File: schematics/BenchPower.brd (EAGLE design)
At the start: 79.7 x 67 mm, 28 parts, among them U1 V_REG_317SINK

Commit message: Reroute another line
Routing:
- net 5VATX: track 100.0 -> 98.9 mm
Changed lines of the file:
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@@
 <wire x1="62.865" y1="51.435" x2="62.865" y2="50.475" width="0.4064" layer="1"/>
 <wire x1="62.865" y1="50.475" x2="62.96" y2="50.38" width="0.4064" layer="1"/>
-<wire x1="60.96" y1="53.34" x2="9.525" y2="53.34" width="0.4064" layer="1"/>
 <wire x1="5.715" y1="10.61" x2="5.89" y2="10.435" width="0.4064" layer="1"/>
-<wire x1="9.525" y1="53.34" x2="6.35" y2="50.165" width="0.4064" layer="1"/>
-<wire x1="6.35" y1="50.165" x2="6.35" y2="10.895" width="0.4064" layer="1"/>
 <wire x1="6.35" y1="10.895" x2="5.89" y2="10.435" width="0.4064" layer="1"/>
+<wire x1="60.96" y1="53.34" x2="27.305" y2="53.34" width="0.4064" layer="1"/>
+<wire x1="27.305" y1="53.34" x2="23.495" y2="49.53" width="0.4064" layer="1"/>
+<wire x1="23.495" y1="49.53" x2="7.62" y2="49.53" width="0.4064" layer="1"/>
+<wire x1="7.62" y1="49.53" x2="6.35" y2="48.26" width="0.4064" layer="1"/>
+<wire x1="6.35" y1="48.26" x2="6.35" y2="10.895" width="0.4064" layer="1"/>
 </signal>
 <signal name="5V$4">

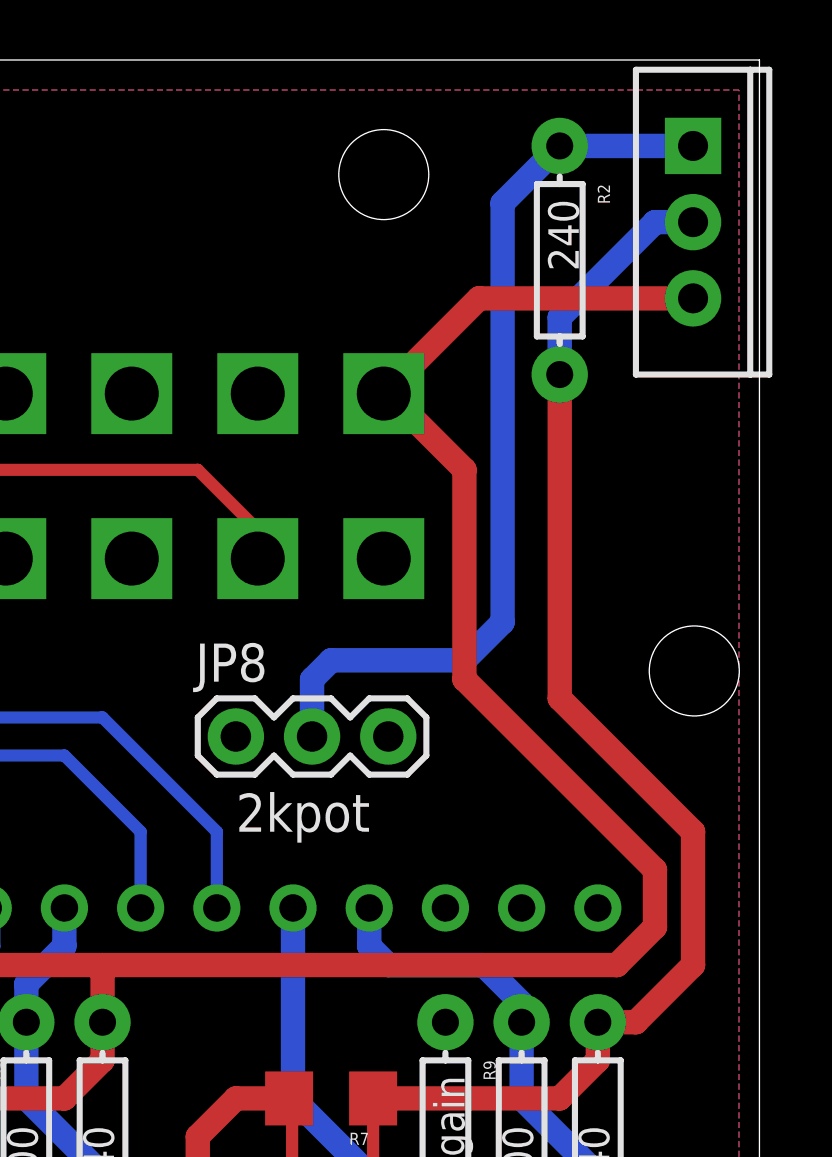
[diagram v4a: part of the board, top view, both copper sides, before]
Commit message: Make 12v or 5v selectable into regulator
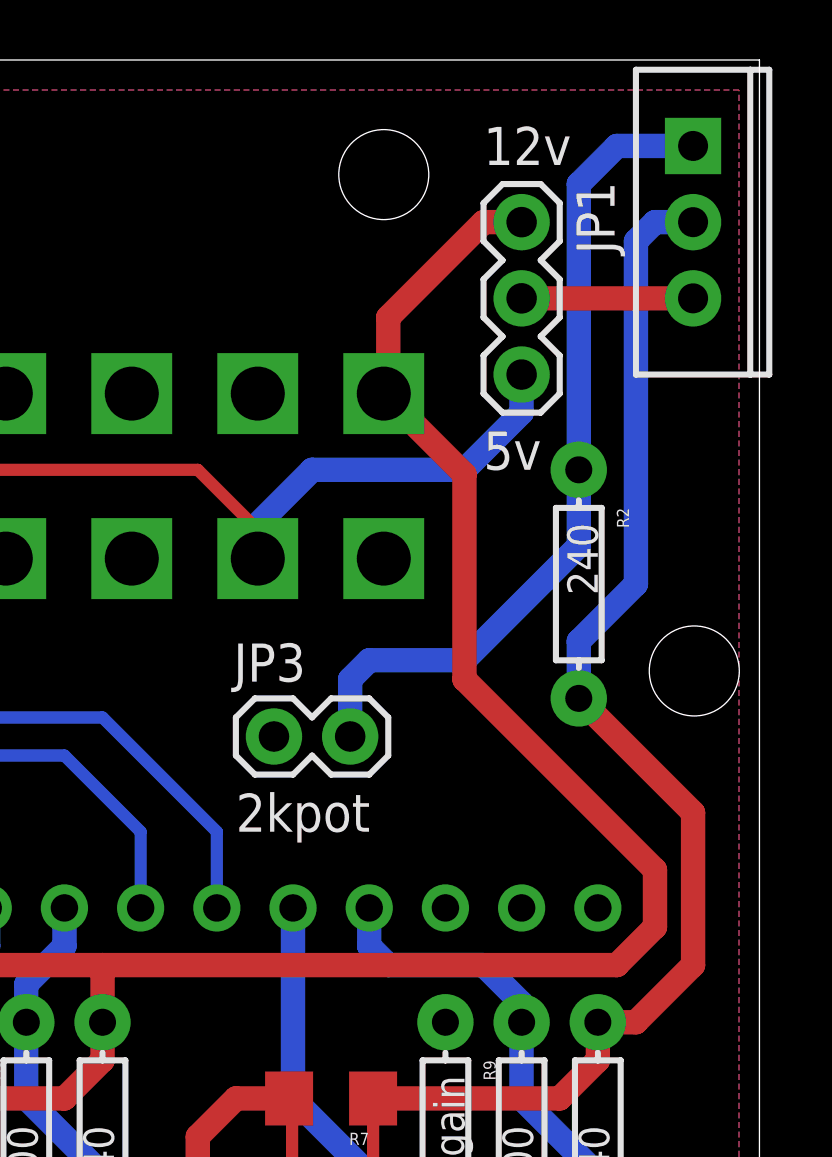
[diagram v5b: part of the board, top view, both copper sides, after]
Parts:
- removed JP8: (no value), SparkFun-Connectors:1X03
- added JP1: (no value), SparkFun-Connectors:1X03
- added JP3: M02PTH, SparkFun-Connectors:1X02
- moved R2 10.8 mm to (73.7, 49.5)
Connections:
- new net REGIN: JP1.2, U1.IN
- net 12VHDR: now also JP1.1; no longer U1.IN
- net 5VATX: now also JP1.3
- net ADJREG1: now also JP3.2; no longer JP8.2
- net GND: now also JP3.1; no longer JP8.1
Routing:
- net 5VATX: track 98.9 -> 111.7 mm
- net REGIN: track 0.00 -> 5.72 mm
- net 12VHDR: track 94.8 -> 91.4 mm
- net ADJREG1: track 30.2 -> 27.8 mm
- net 12VREG: track 45.3 -> 44.8 mm
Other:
- board text added: "5v"
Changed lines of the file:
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@@
 <text x="62.23" y="41.275" size="1.27" layer="21" font="vector">2kpot</text>
 <text x="24.765" y="62.23" size="1.27" layer="21" font="vector" rot="R90">lcd</text>
+<text x="70.485" y="63.5" size="1.27" layer="21" font="vector">12v</text>
+<text x="70.485" y="53.34" size="1.27" layer="21" font="vector">5v</text>
 </plain>
 <attributes>
@@
 <element name="U1" library="SparkFun-PowerIC" package="TO220-ADJ" value="V_REG_317SINK" x="77.47" y="61.595" rot="R270"/>
 <element name="R1" library="SparkFun-Passives" package="AXIAL-0.3" value="1000" x="31.75" y="31.75" rot="R270"/>
-<element name="R2" library="SparkFun-Passives" package="AXIAL-0.3" value="240" x="73.025" y="60.325" rot="R270"/>
+<element name="R2" library="SparkFun-Passives" package="AXIAL-0.3" value="240" x="73.66" y="49.53" rot="R270"/>
 <element name="U$3" library="desjardins" package="LOGO" value="" x="1.905" y="58.42"/>
 <element name="LCD" library="desjardins" package="DT162C" value="16X2LCDDT162C" x="40.01" y="31.135"/>
@@
 <element name="JP6" library="SparkFun-Connectors" package="1X02" value="M02PTH" x="31.75" y="2.54"/>
 <element name="JP7" library="SparkFun-Connectors" package="USB-A-S" value="USB-A-S" x="8.89" y="6.985" rot="R90"/>
-<element name="JP8" library="SparkFun-Connectors" package="1X03" value="" x="62.23" y="44.45"/>
+<element name="JP1" library="SparkFun-Connectors" package="1X03" value="" x="71.755" y="61.595" rot="R270"/>
+<element name="JP3" library="SparkFun-Connectors" package="1X02" value="M02PTH" x="63.5" y="44.45"/>
 </elements>
 <signals>
@@
 <contactref element="JP2" pad="2"/>
 <contactref element="JP7" pad="GND"/>
-<contactref element="JP8" pad="1"/>
+<contactref element="JP3" pad="1"/>
 </signal>
 <signal name="5VSB">
@@
 <contactref element="R1" pad="P$1"/>
 <contactref element="R6" pad="1"/>
-<contactref element="U1" pad="IN"/>
 <contactref element="U5" pad="3"/>
 <wire x1="76.2" y1="38.1" x2="74.93" y2="36.83" width="0.8128" layer="1"/>
 <wire x1="74.93" y1="36.83" x2="57.785" y2="36.83" width="0.8128" layer="1"/>
-<wire x1="67.16" y1="55.88" x2="67.31" y2="55.88" width="0.8128" layer="1"/>
-<wire x1="67.31" y1="55.88" x2="69.85" y2="53.34" width="0.8128" layer="1"/>
 <wire x1="76.2" y1="40.005" x2="76.2" y2="38.1" width="0.8128" layer="1"/>
 <wire x1="40.005" y1="36.83" x2="38.735" y2="38.1" width="0.8128" layer="1"/>
 <wire x1="38.735" y1="38.1" x2="38.735" y2="38.735" width="0.8128" layer="1"/>
-<wire x1="69.85" y1="53.34" x2="69.85" y2="46.355" width="0.8128" layer="1"/>
 <wire x1="69.85" y1="46.355" x2="76.2" y2="40.005" width="0.8128" layer="1"/>
 <wire x1="50.295" y1="32.385" x2="50.295" y2="29.6249" width="0.4064" layer="1"/>
@@
 <wire x1="31.75" y1="35.56" x2="35.56" y2="35.56" width="0.4064" layer="1"/>
 <wire x1="35.56" y1="35.56" x2="38.735" y2="38.735" width="0.4064" layer="1"/>
-<wire x1="77.47" y1="59.055" x2="70.335" y2="59.055" width="0.8128" layer="1"/>
-<wire x1="70.335" y1="59.055" x2="67.16" y2="55.88" width="0.8128" layer="1"/>
+<contactref element="JP1" pad="1"/>
+<wire x1="71.755" y1="61.595" x2="70.485" y2="61.595" width="0.8128" layer="1"/>
+<wire x1="70.485" y1="61.595" x2="67.31" y2="58.42" width="0.8128" layer="1"/>
+<wire x1="67.31" y1="58.42" x2="67.31" y2="56.03" width="0.8128" layer="1"/>
+<wire x1="67.31" y1="56.03" x2="67.16" y2="55.88" width="0.8128" layer="1"/>
+<wire x1="69.85" y1="46.355" x2="69.85" y2="53.19" width="0.8128" layer="1"/>
+<wire x1="69.85" y1="53.19" x2="67.16" y2="55.88" width="0.8128" layer="1"/>
 </signal>
 <signal name="N$1">
@@
 <wire x1="74.295" y1="34.925" x2="75.565" y2="34.925" width="0.8128" layer="1"/>
 <wire x1="75.565" y1="34.925" x2="77.47" y2="36.83" width="0.8128" layer="1"/>
-<wire x1="77.47" y1="36.83" x2="77.47" y2="41.275" width="0.8128" layer="1"/>
-<wire x1="77.47" y1="41.275" x2="73.025" y2="45.72" width="0.8128" layer="1"/>
-<wire x1="73.025" y1="45.72" x2="73.025" y2="56.515" width="0.8128" layer="1"/>
-<wire x1="73.025" y1="56.515" x2="73.025" y2="58.42" width="0.8128" layer="16"/>
-<wire x1="73.025" y1="58.42" x2="76.2" y2="61.595" width="0.8128" layer="16"/>
+<wire x1="77.47" y1="36.83" x2="77.47" y2="41.91" width="0.8128" layer="1"/>
 <wire x1="76.2" y1="61.595" x2="77.47" y2="61.595" width="0.8128" layer="16"/>
 <wire x1="66.805" y1="32.385" x2="66.805" y2="29.6249" width="0.4064" layer="1"/>
 <wire x1="66.805" y1="29.6249" x2="66.7051" y2="29.525" width="0.4064" layer="1"/>
+<wire x1="76.2" y1="61.595" x2="75.565" y2="60.96" width="0.8128" layer="16"/>
+<wire x1="75.565" y1="60.96" x2="75.565" y2="49.53" width="0.8128" layer="16"/>
+<wire x1="75.565" y1="49.53" x2="73.66" y2="47.625" width="0.8128" layer="16"/>
+<wire x1="73.66" y1="47.625" x2="73.66" y2="45.72" width="0.8128" layer="16"/>
+<wire x1="77.47" y1="41.91" x2="73.66" y2="45.72" width="0.8128" layer="1"/>
 </signal>
 <signal name="ADJREG1">
 <contactref element="U1" pad="ADJ"/>
 <contactref element="R2" pad="P$1"/>
-<contactref element="JP8" pad="2"/>
-<wire x1="73.025" y1="64.135" x2="77.47" y2="64.135" width="0.8128" layer="16"/>
-<wire x1="71.12" y1="62.23" x2="73.025" y2="64.135" width="0.8128" layer="16"/>
-<wire x1="71.12" y1="62.23" x2="71.12" y2="48.26" width="0.8128" layer="16"/>
-<wire x1="71.12" y1="48.26" x2="69.85" y2="46.99" width="0.8128" layer="16"/>
-<wire x1="69.85" y1="46.99" x2="65.405" y2="46.99" width="0.8128" layer="16"/>
-<wire x1="65.405" y1="46.99" x2="64.77" y2="46.355" width="0.8128" layer="16"/>
-<wire x1="64.77" y1="46.355" x2="64.77" y2="44.45" width="0.8128" layer="16"/>
+<wire x1="73.66" y1="62.865" x2="74.93" y2="64.135" width="0.8128" layer="16"/>
+<wire x1="74.93" y1="64.135" x2="77.47" y2="64.135" width="0.8128" layer="16"/>
+<contactref element="JP3" pad="2"/>
+<wire x1="69.85" y1="46.99" x2="66.675" y2="46.99" width="0.8128" layer="16"/>
+<wire x1="66.675" y1="46.99" x2="66.04" y2="46.355" width="0.8128" layer="16"/>
+<wire x1="66.04" y1="46.355" x2="66.04" y2="44.45" width="0.8128" layer="16"/>
+<wire x1="69.85" y1="46.99" x2="73.66" y2="50.8" width="0.8128" layer="16"/>
+<wire x1="73.66" y1="50.8" x2="73.66" y2="53.34" width="0.8128" layer="16"/>
+<wire x1="73.66" y1="62.865" x2="73.66" y2="53.34" width="0.8128" layer="16"/>
 </signal>
 <signal name="5VARDU">
@@
 <wire x1="7.62" y1="49.53" x2="6.35" y2="48.26" width="0.4064" layer="1"/>
 <wire x1="6.35" y1="48.26" x2="6.35" y2="10.895" width="0.4064" layer="1"/>
+<contactref element="JP1" pad="3"/>
+<wire x1="64.77" y1="53.34" x2="62.865" y2="51.435" width="0.8128" layer="16"/>
+<wire x1="62.865" y1="51.435" x2="62.865" y2="50.475" width="0.8128" layer="16"/>
+<wire x1="62.865" y1="50.475" x2="62.96" y2="50.38" width="0.8128" layer="16"/>
+<wire x1="64.77" y1="53.34" x2="69.85" y2="53.34" width="0.8128" layer="16"/>
+<wire x1="69.85" y1="53.34" x2="71.755" y2="55.245" width="0.8128" layer="16"/>
+<wire x1="71.755" y1="55.245" x2="71.755" y2="56.515" width="0.8128" layer="16"/>
 </signal>
 <signal name="5V$4">
 <contactref element="ATXCONN" pad="P$20"/>
 </signal>
+<signal name="REGIN">
+<contactref element="U1" pad="IN"/>
+<contactref element="JP1" pad="2"/>
+<wire x1="71.755" y1="59.055" x2="77.47" y2="59.055" width="0.8128" layer="1"/>
+</signal>
 </signals>

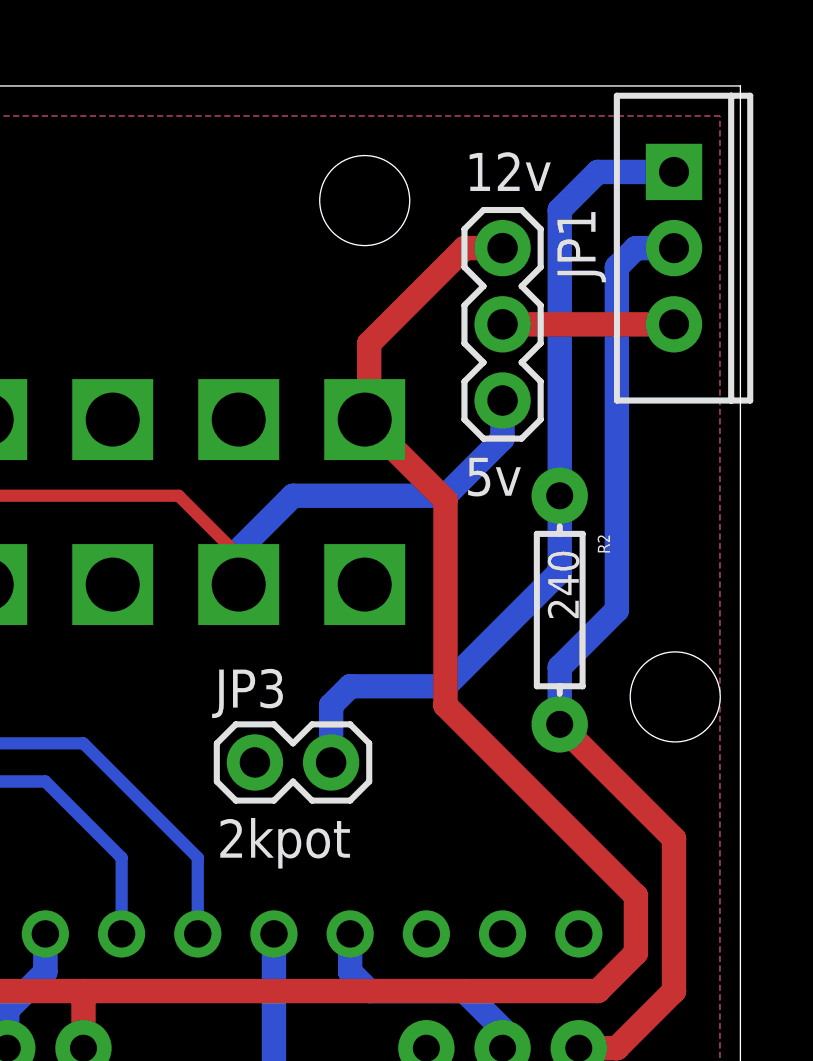
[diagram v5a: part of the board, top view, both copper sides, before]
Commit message: Move 2k pot header
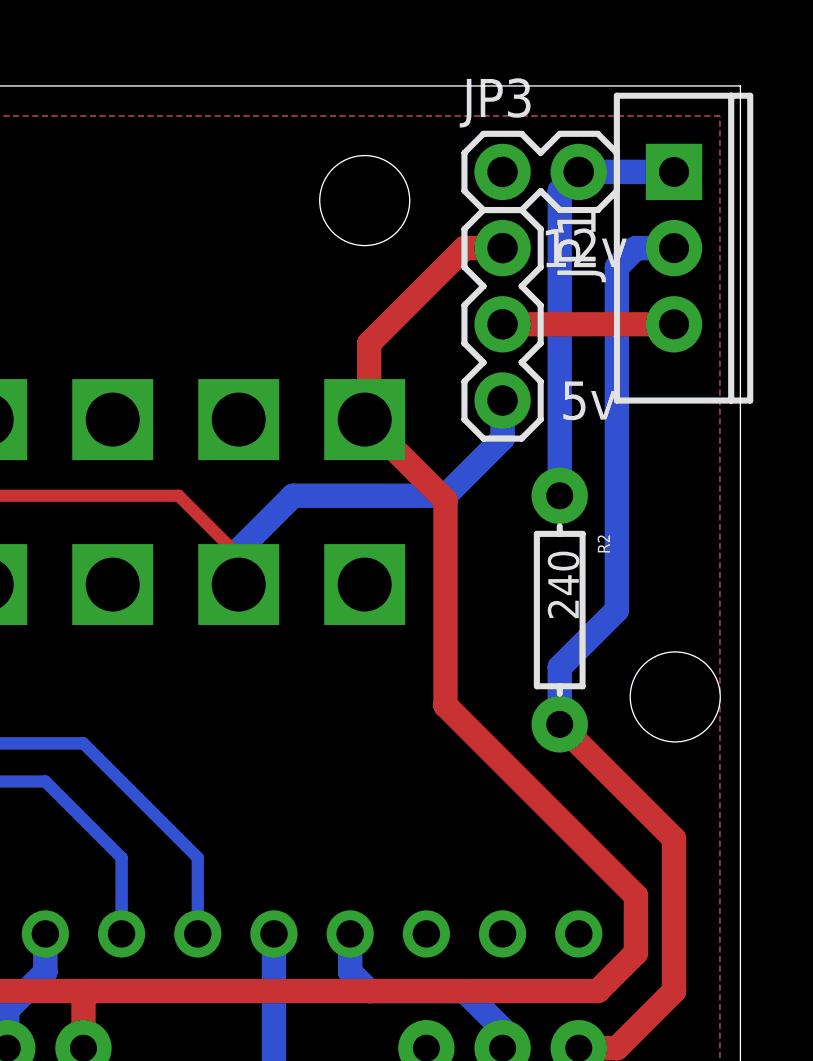
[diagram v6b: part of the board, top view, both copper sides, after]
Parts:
- moved JP3 21.3 mm to (71.8, 64.1)
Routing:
- net ADJREG1: track 27.8 -> 14.2 mm
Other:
- board text added: "2k"
- board text removed: "2kpot"
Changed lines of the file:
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@@
 <text x="73.025" y="5.715" size="1.27" layer="21" font="vector" rot="R180">adj</text>
 <text x="73.025" y="3.175" size="1.27" layer="21" font="vector" rot="R180">gnd</text>
-<text x="62.23" y="41.275" size="1.27" layer="21" font="vector">2kpot</text>
+<text x="70.485" y="65.405" size="1.27" layer="22" font="vector" rot="R180">2k</text>
 <text x="24.765" y="62.23" size="1.27" layer="21" font="vector" rot="R90">lcd</text>
-<text x="70.485" y="63.5" size="1.27" layer="21" font="vector">12v</text>
-<text x="70.485" y="53.34" size="1.27" layer="21" font="vector">5v</text>
+<text x="73.025" y="60.96" size="1.27" layer="21" font="vector">12v</text>
+<text x="73.66" y="55.88" size="1.27" layer="21" font="vector">5v</text>
 </plain>
 <attributes>
@@
 <element name="JP7" library="SparkFun-Connectors" package="USB-A-S" value="USB-A-S" x="8.89" y="6.985" rot="R90"/>
 <element name="JP1" library="SparkFun-Connectors" package="1X03" value="" x="71.755" y="61.595" rot="R270"/>
-<element name="JP3" library="SparkFun-Connectors" package="1X02" value="M02PTH" x="63.5" y="44.45"/>
+<element name="JP3" library="SparkFun-Connectors" package="1X02" value="M02PTH" x="71.755" y="64.135"/>
 </elements>
 <signals>
@@
 <contactref element="U1" pad="ADJ"/>
 <contactref element="R2" pad="P$1"/>
-<wire x1="73.66" y1="62.865" x2="74.93" y2="64.135" width="0.8128" layer="16"/>
-<wire x1="74.93" y1="64.135" x2="77.47" y2="64.135" width="0.8128" layer="16"/>
 <contactref element="JP3" pad="2"/>
-<wire x1="69.85" y1="46.99" x2="66.675" y2="46.99" width="0.8128" layer="16"/>
-<wire x1="66.675" y1="46.99" x2="66.04" y2="46.355" width="0.8128" layer="16"/>
-<wire x1="66.04" y1="46.355" x2="66.04" y2="44.45" width="0.8128" layer="16"/>
-<wire x1="69.85" y1="46.99" x2="73.66" y2="50.8" width="0.8128" layer="16"/>
-<wire x1="73.66" y1="50.8" x2="73.66" y2="53.34" width="0.8128" layer="16"/>
-<wire x1="73.66" y1="62.865" x2="73.66" y2="53.34" width="0.8128" layer="16"/>
+<wire x1="77.47" y1="64.135" x2="74.295" y2="64.135" width="0.8128" layer="16"/>
+<wire x1="74.295" y1="64.135" x2="73.66" y2="63.5" width="0.8128" layer="16"/>
+<wire x1="73.66" y1="63.5" x2="73.66" y2="53.34" width="0.8128" layer="16"/>
 </signal>
 <signal name="5VARDU">
